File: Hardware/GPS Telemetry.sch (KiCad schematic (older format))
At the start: 0 parts

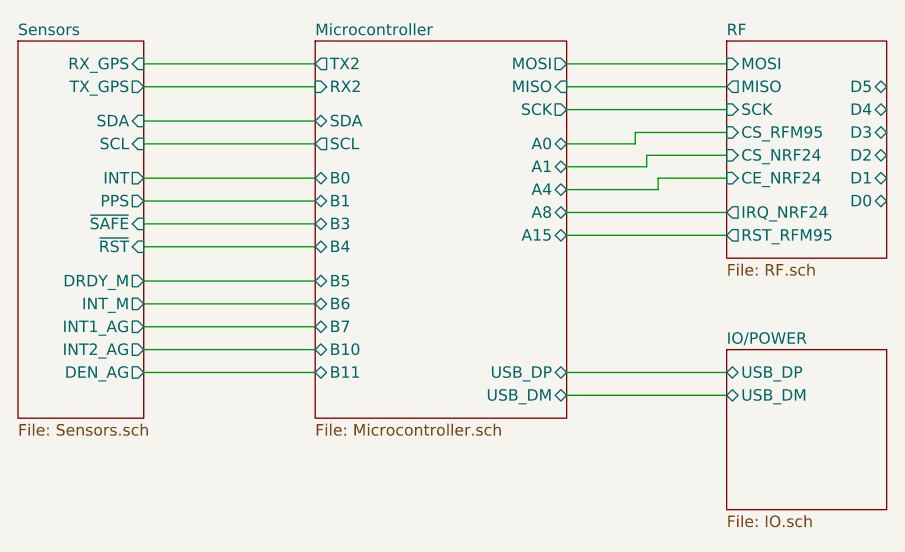
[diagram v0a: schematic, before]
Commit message: Rearranged pins so Serial and I2C are available for external use.
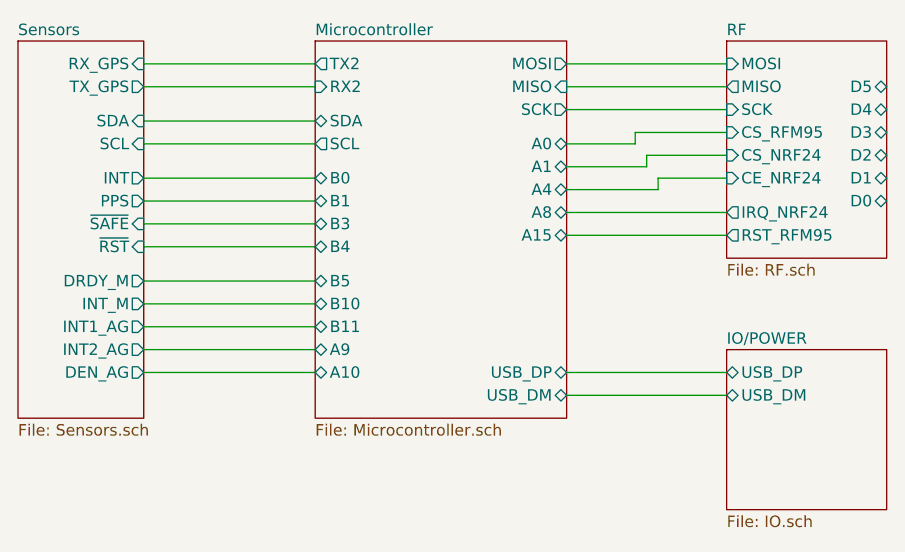
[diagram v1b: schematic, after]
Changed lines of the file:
@@
 F14 "B4" B L 5600 4050 50
 F15 "B5" B L 5600 4200 50
-F16 "B6" B L 5600 4300 50
-F17 "B7" B L 5600 4400 50
-F18 "B10" B L 5600 4500 50
-F19 "B11" B L 5600 4600 50
-F20 "A0" B R 6700 3600 50
-F21 "A1" B R 6700 3700 50
-F22 "A4" B R 6700 3800 50
-F23 "A8" B R 6700 3900 50
-F24 "A15" B R 6700 4000 50
+F16 "B10" B L 5600 4300 50
+F17 "B11" B L 5600 4400 50
+F18 "A0" B R 6700 3600 50
+F19 "A1" B R 6700 3700 50
+F20 "A4" B R 6700 3800 50
+F21 "A8" B R 6700 3900 50
+F22 "A15" B R 6700 4000 50
+F23 "A9" B L 5600 4500 50
+F24 "A10" B L 5600 4600 50
 $EndSheet
 $Sheet
